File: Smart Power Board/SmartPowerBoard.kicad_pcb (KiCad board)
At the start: 4 copper layers, 41.8 x 41.5 mm, 94 parts, among them J1 430450200, J2 USB_C_Receptacle_USB2.0_16P, J3 430450200, J4 Conn_01x02_Socket, J5 Screw_Terminal_01x02, J6 Screw_Terminal_01x02, Q1 PMOS, Q2 NMOS, SW1 SW_Push, SW2 SW_Push, SW3 SW_Push, U1 INA3221, U2 X096-2864TMBAG01-H30, U4 TPS56C230RJER, U5 TPS56C230RJER, U6 RP2040, U7 W25Q32JVSS, Y1 FL1200138

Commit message: Feat[SmartPowerBoard]: New Layout
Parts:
- removed J4: Conn_01x02_Socket, Connector_Molex:Molex_PicoBlade_53047-0210_1x02_P1.25mm_Vertical
- removed J6: Screw_Terminal_01x02, 282837_2:TE_282837-2
- J3: value 430450200 -> 430450601; footprint ul_430450200:CON_430450200_MOL -> 430450601:MOLEX_430450601
- J5: value Screw_Terminal_01x02 -> 430450400; footprint 282837_2:TE_282837-2 -> 430450400:MOLEX_430450400
- moved J2 37.8 mm to (169.2, 122.0), turned to 0 degrees
- moved J5 33.9 mm to (154.2, 85.0), turned to 180 degrees
- moved Y1 28.1 mm to (160.6, 123.3), turned to 90 degrees
- moved R10 27.5 mm to (167.2, 116.6), turned to 180 degrees
- moved R11 27.5 mm to (171.1, 116.6)
- moved C34 26.1 mm to (159.3, 119.9), turned to 180 degrees
- moved R34 26.0 mm to (158.0, 118.2), turned to 90 degrees
- moved C33 25.1 mm to (161.3, 121.0), turned to 180 degrees
- moved R38 25.0 mm to (156.0, 112.0), turned to 90 degrees
- moved R35 24.8 mm to (159.0, 118.2), turned to 90 degrees
- moved R37 24.5 mm to (156.0, 110.0), turned to -90 degrees
- moved R19 24.0 mm to (161.3, 119.9), turned to 180 degrees
- moved C12 22.9 mm to (160.9, 118.4), turned to 90 degrees
- moved C13 22.6 mm to (157.3, 107.9), turned to -90 degrees
- moved SW3 22.4 mm to (168.8, 85.9), turned to 180 degrees
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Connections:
- J1 pad 1: GND -> unconnected-(J1-Pad1)
- J3 pad 2: /Triple Channel Monitor/12V_{OUT} -> GND
- J5 pad 2: /Triple Channel Monitor/5V_{OUT} -> GND
- R13 pad 4: /Buck Converter 5V/V_{OUT} -> /Triple Channel Monitor/5V_{IN}
- R14 pad 1: /12V_{IN} -> /Triple Channel Monitor/12V_{IN}
- R14 pad 2: Net-(U1-IN-1) -> Net-(U1-IN-3)
- R14 pad 3: Net-(U1-IN+1) -> Net-(U1-IN+3)
- R15 pad 2: Net-(U1-IN-3) -> Net-(U1-IN-1)
- R15 pad 3: Net-(U1-IN+3) -> Net-(U1-IN+1)
- R27 pad 2: Net-(U5-VCC) -> /Buck Converter 3.3V/V_{CC}
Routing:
- net /12V_{IN}: track 53.8 -> 0.00 mm, vias 3 -> 0
- net /3.3V_{IN}: track 23.3 -> 0.00 mm, vias 2 -> 0
- net /MCU/USB_M: track 22.6 -> 0.00 mm
- net /Triple Channel Monitor/3.3V_{IN}: track 21.9 -> 0.00 mm, vias 3 -> 0
- net /Triple Channel Monitor/12V_{OUT}: track 20.8 -> 0.00 mm, vias 1 -> 0
- net /Triple Channel Monitor/5V_{OUT}: track 19.0 -> 0.00 mm, vias 1 -> 0
- net /MCU/USB_P: track 15.9 -> 0.00 mm
- net /Buck Converter 5V/V_{OUT}: track 13.5 -> 0.00 mm, vias 2 -> 0
- net /Triple Channel Monitor/3.3V: track 13.5 -> 0.02 mm, vias 3 -> 1
- net /MCU/3.3V: track 12.9 -> 0.00 mm, vias 1 -> 0
- net Net-(Q1-G): track 11.7 -> 0.00 mm
- net Net-(U5-VCC): track 10.7 -> 0.00 mm, vias 2 -> 0
- net /MCU/XIN: track 8.49 -> 0.00 mm
- net Net-(U6-USB_DM): track 7.72 -> 0.00 mm, vias 2 -> 0
- net Net-(U6-USB_DP): track 7.31 -> 0.00 mm, vias 2 -> 0
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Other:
- board size 41.8 x 41.5 mm -> 38.7 x 49.5 mm
- board text added: "YOU CAN CHANGE THIS"

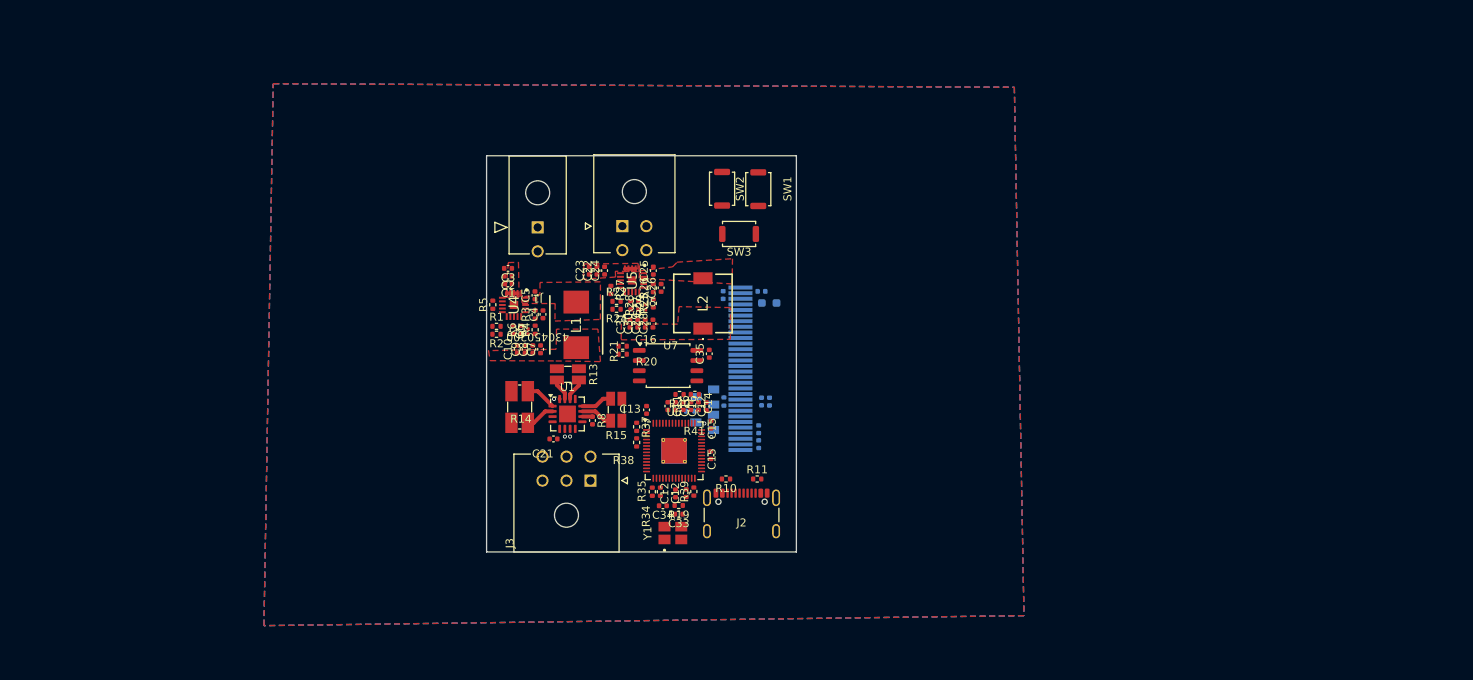
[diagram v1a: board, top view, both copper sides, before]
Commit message: Feat[SmartPowerBoard]: Organized Schematic and New Buck
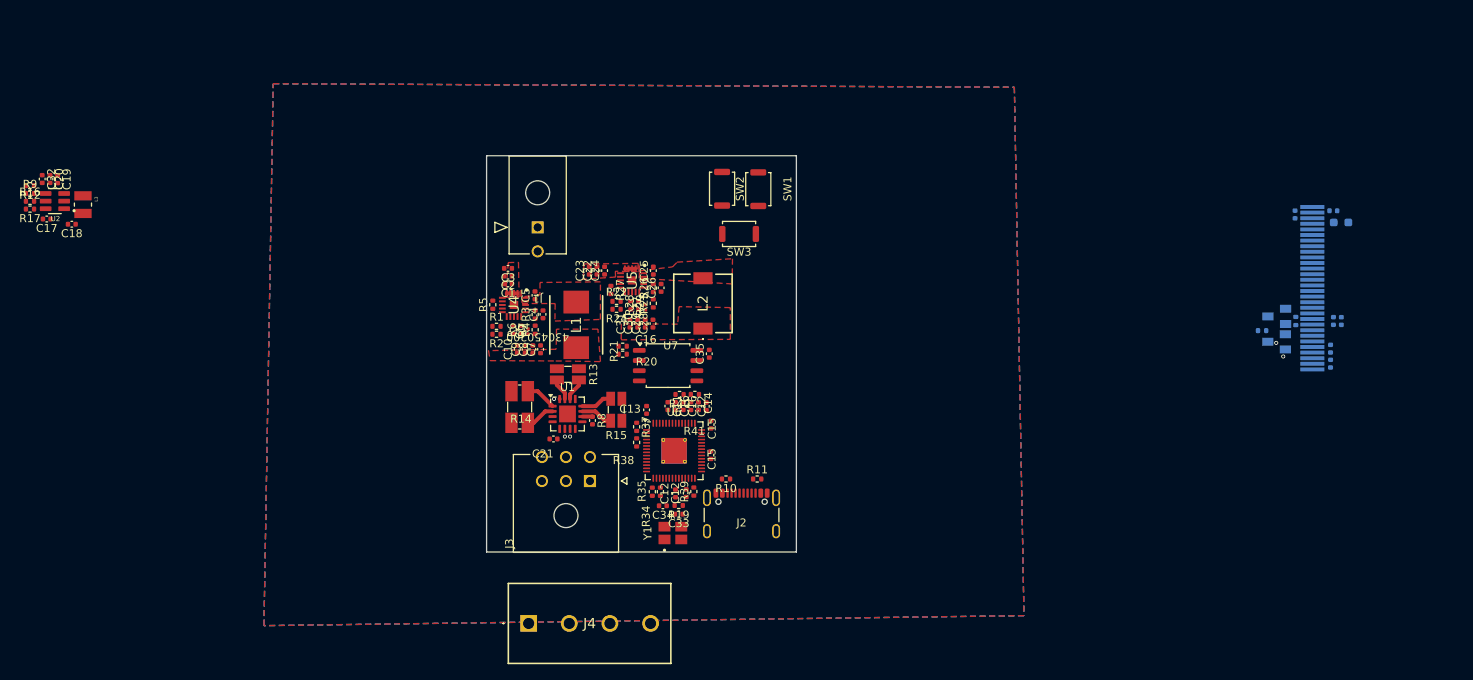
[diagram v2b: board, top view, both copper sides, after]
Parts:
- removed J5: 430450400, 430450400:MOLEX_430450400
- added C17: 0.1uF, Capacitor_SMD:C_0402_1005Metric, F.Cu at (82.3, 84.1)
- added C18: 47uF, Capacitor_SMD:C_0402_1005Metric, F.Cu at (85.4, 84.7)
- added C19: 22uF, Capacitor_SMD:C_0402_1005Metric, F.Cu at (83.7, 79.1)
- added C20: 22uF, Capacitor_SMD:C_0402_1005Metric, F.Cu at (82.7, 79.1)
- added C32: 0.1uF, Capacitor_SMD:C_0402_1005Metric, F.Cu at (81.7, 79.1)
- added J4: Screw_Terminal_01x04, 282857-4_KiCad:2828574, F.Cu at (142.5, 134.6)
- added L3: MLP2520S3R3ST0S1, MLP2520S3R3ST0S1:INDC2520X120N, F.Cu at (86.8, 82.3)
- added R12: 10k, Resistor_SMD:R_0402_1005Metric, F.Cu at (80.2, 79.9)
- added R16: 102k, Resistor_SMD:R_0402_1005Metric, F.Cu at (80.2, 81.9)
- added R17: 51k, Resistor_SMD:R_0402_1005Metric, F.Cu at (80.2, 82.8)
- added R9: 33.2k, Resistor_SMD:R_0402_1005Metric, F.Cu at (80.2, 80.9)
- added U2: TPS561201DDCR, TPS561201DDCR:SOT95P280X110-6N, F.Cu at (83.3, 81.8)
- moved Q2 72.2 mm to (236.1, 96.2)
- moved R18 72.2 mm to (238.4, 96.8)
- moved C17 72.2 mm to (243.1, 83.0)
- moved C18 72.2 mm to (238.3, 83.5)
- moved C19 72.2 mm to (242.8, 102.2)
- moved C20 72.2 mm to (242.8, 100.3)
- moved C32 72.2 mm to (244.1, 96.8)
- moved C36 72.2 mm to (243.1, 96.8)
- moved Q1 72.2 mm to (236.0, 99.4)
- moved R12 72.2 mm to (234.2, 98.0)
- moved R9 72.2 mm to (244.1, 84.5)
- moved U2 72.2 mm to (241.3, 92.8)
- moved J3 0.08 mm to (150.2, 116.8)
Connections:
- net /MCU/5V renamed /MCU/5V_{IN}
- C1 pad 1: /Buck Converter 5V/V_{IN} -> /12V_{IN}
- C10 pad 1: /Buck Converter 5V/V_{OUT} -> /Buck Converter 5V/5V_{OUT}
- C13 pad 2: /MCU/3.3V -> /MCU/3.3V_{CC}
- C14 pad 2: /MCU/3.3V -> /MCU/3.3V_{CC}
- C15 pad 2: /MCU/3.3V -> /MCU/3.3V_{CC}
- C16 pad 2: /MCU/3.3V -> /MCU/3.3V_{CC}
- C2 pad 1: /Buck Converter 5V/V_{IN} -> /12V_{IN}
- C21 pad 2: /Triple Channel Monitor/3.3V -> /MCU/3.3V_{CC}
- C22 pad 1: /Buck Converter 3.3V/V_{IN} -> /12V_{IN}
- C23 pad 1: /Buck Converter 3.3V/V_{IN} -> /12V_{IN}
- C24 pad 1: /Buck Converter 3.3V/V_{IN} -> /12V_{IN}
- C27 pad 1: /Buck Converter 3.3V/V_{OUT} -> /Buck Converter 3.3V/3.3V_{OUT}
- C28 pad 1: /Buck Converter 3.3V/V_{OUT} -> /Buck Converter 3.3V/3.3V_{OUT}
- C29 pad 1: /Buck Converter 3.3V/V_{OUT} -> /Buck Converter 3.3V/3.3V_{OUT}
- C3 pad 1: /Buck Converter 5V/V_{IN} -> /12V_{IN}
- C30 pad 1: /Buck Converter 3.3V/V_{OUT} -> /Buck Converter 3.3V/3.3V_{OUT}
- C31 pad 1: /Buck Converter 3.3V/V_{OUT} -> /Buck Converter 3.3V/3.3V_{OUT}
- C35 pad 2: /MCU/3.3V -> /MCU/3.3V_{CC}
- C6 pad 1: /Buck Converter 5V/V_{OUT} -> /Buck Converter 5V/5V_{OUT}
- C7 pad 1: /Buck Converter 5V/V_{OUT} -> /Buck Converter 5V/5V_{OUT}
- C8 pad 1: /Buck Converter 5V/V_{OUT} -> /Buck Converter 5V/5V_{OUT}
- C9 pad 1: /Buck Converter 5V/V_{OUT} -> /Buck Converter 5V/5V_{OUT}
- J1 pad 1: unconnected-(J1-Pad1) -> GND
- J3 pad 4: /3.3V_{IN} -> /12V_{OUT}
- J3 pad 5: /5V_{OUT} -> /12V_{OUT}
- J3 pad 6: /12V_{IN} -> /12V_{OUT}
- L1 pad 2: /Buck Converter 5V/V_{OUT} -> /Buck Converter 5V/5V_{OUT}
- L2 pad 1: /Buck Converter 3.3V/V_{OUT} -> /Buck Converter 3.3V/3.3V_{OUT}
- R1 pad 1: /Buck Converter 5V/V_{IN} -> /12V_{IN}
- R13 pad 4: /Triple Channel Monitor/5V_{IN} -> /Buck Converter 5V/5V_{OUT}
- R14 pad 1: /Triple Channel Monitor/12V_{IN} -> /12V_{IN}
- R15 pad 4: /Triple Channel Monitor/3.3V_{IN} -> /Buck Converter 3.3V/3.3V_{OUT}
- R21 pad 2: /MCU/3.3V -> /MCU/3.3V_{CC}
- R22 pad 1: /Buck Converter 3.3V/V_{IN} -> /12V_{IN}
- R28 pad 1: /Buck Converter 3.3V/V_{OUT} -> /Buck Converter 3.3V/3.3V_{OUT}
- R34 pad 1: /MCU/3.3V -> /MCU/3.3V_{CC}
- R35 pad 1: /MCU/3.3V -> /MCU/3.3V_{CC}
- R37 pad 1: /MCU/3.3V -> /MCU/3.3V_{CC}
- R37 pad 2: /MCU/SDA -> /MCU/SCL
- R38 pad 1: /MCU/3.3V -> /MCU/3.3V_{CC}
- R38 pad 2: /MCU/SCL -> /MCU/SDA
- R39 pad 1: /MCU/3.3V -> /MCU/3.3V_{CC}
- R6 pad 1: /Buck Converter 5V/V_{OUT} -> /Buck Converter 5V/5V_{OUT}
- R8 pad 2: /Triple Channel Monitor/3.3V -> /MCU/3.3V_{CC}
- U1 pad 16: /Triple Channel Monitor/3.3V -> /MCU/3.3V_{CC}
- U1 pad 4: /Triple Channel Monitor/3.3V -> /MCU/3.3V_{CC}
- U1 pad 6: /Triple Channel Monitor/SCL -> /MCU/SCL
- U1 pad 7: /Triple Channel Monitor/SDA -> /MCU/SDA
- U1 pad 8: /Triple Channel Monitor/WARN -> /MCU/WARN
- U1 pad 9: /Triple Channel Monitor/CRIT -> /MCU/CRIT
- U4 pad 2: /Buck Converter 5V/V_{IN} -> /12V_{IN}
- U4 pad 3: /Buck Converter 5V/V_{IN} -> /12V_{IN}
- U4 pad 4: /Buck Converter 5V/V_{IN} -> /12V_{IN}
- U4 pad 5: /Buck Converter 5V/V_{IN} -> /12V_{IN}
- U5 pad 2: /Buck Converter 3.3V/V_{IN} -> /12V_{IN}
- U5 pad 3: /Buck Converter 3.3V/V_{IN} -> /12V_{IN}
- U5 pad 4: /Buck Converter 3.3V/V_{IN} -> /12V_{IN}
- U5 pad 5: /Buck Converter 3.3V/V_{IN} -> /12V_{IN}
- U6 pad 1: /MCU/3.3V -> /MCU/3.3V_{CC}
- U6 pad 10: /MCU/3.3V -> /MCU/3.3V_{CC}
- U6 pad 2: /MCU/SDA -> /MCU/SCL
- U6 pad 22: /MCU/3.3V -> /MCU/3.3V_{CC}
- U6 pad 3: /MCU/SCL -> /MCU/SDA
- U6 pad 33: /MCU/3.3V -> /MCU/3.3V_{CC}
- U6 pad 42: /MCU/3.3V -> /MCU/3.3V_{CC}
- U6 pad 43: /MCU/3.3V -> /MCU/3.3V_{CC}
- U6 pad 44: /MCU/3.3V -> /MCU/3.3V_{CC}
- U6 pad 48: /MCU/3.3V -> /MCU/3.3V_{CC}
- U6 pad 49: /MCU/3.3V -> /MCU/3.3V_{CC}
- U7 pad 8: /MCU/3.3V -> /MCU/3.3V_{CC}
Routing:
- net /12V_{IN}: track 0.00 -> 2.63 mm
- net /Buck Converter 5V/V_{IN}: track 1.31 -> 0.00 mm
- net /Buck Converter 3.3V/V_{IN}: track 1.31 -> 0.00 mm
- net /Triple Channel Monitor/3.3V: track 0.02 -> 0.00 mm, vias 1 -> 0
- net /MCU/3.3V_{CC}: track 0.00 -> 0.02 mm, vias 0 -> 1
- net /Triple Channel Monitor/SDA: vias 1 -> 0
- net /Triple Channel Monitor/SCL: vias 1 -> 0
- net /MCU/SDA: vias 0 -> 1
- net /MCU/SCL: vias 0 -> 1
- added copper zone on F.Cu, net /12V_{IN}
- added copper zone on F.Cu, net /Buck Converter 3.3V/3.3V_{OUT}
- added copper zone on F.Cu, net /Buck Converter 5V/5V_{OUT}
- removed copper zone on F.Cu, net /Buck Converter 3.3V/V_{IN}
- removed copper zone on F.Cu, net /Buck Converter 3.3V/V_{OUT}
- removed copper zone on F.Cu, net /Buck Converter 5V/V_{IN}
- removed copper zone on F.Cu, net /Buck Converter 5V/V_{OUT}
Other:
- board text added: "Add mini buck"
- board text added: "NEW OLED"
- board text removed: "YOU CAN CHANGE THIS"

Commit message: Feat[SmartPowerBoard]: Internal Power + OLED
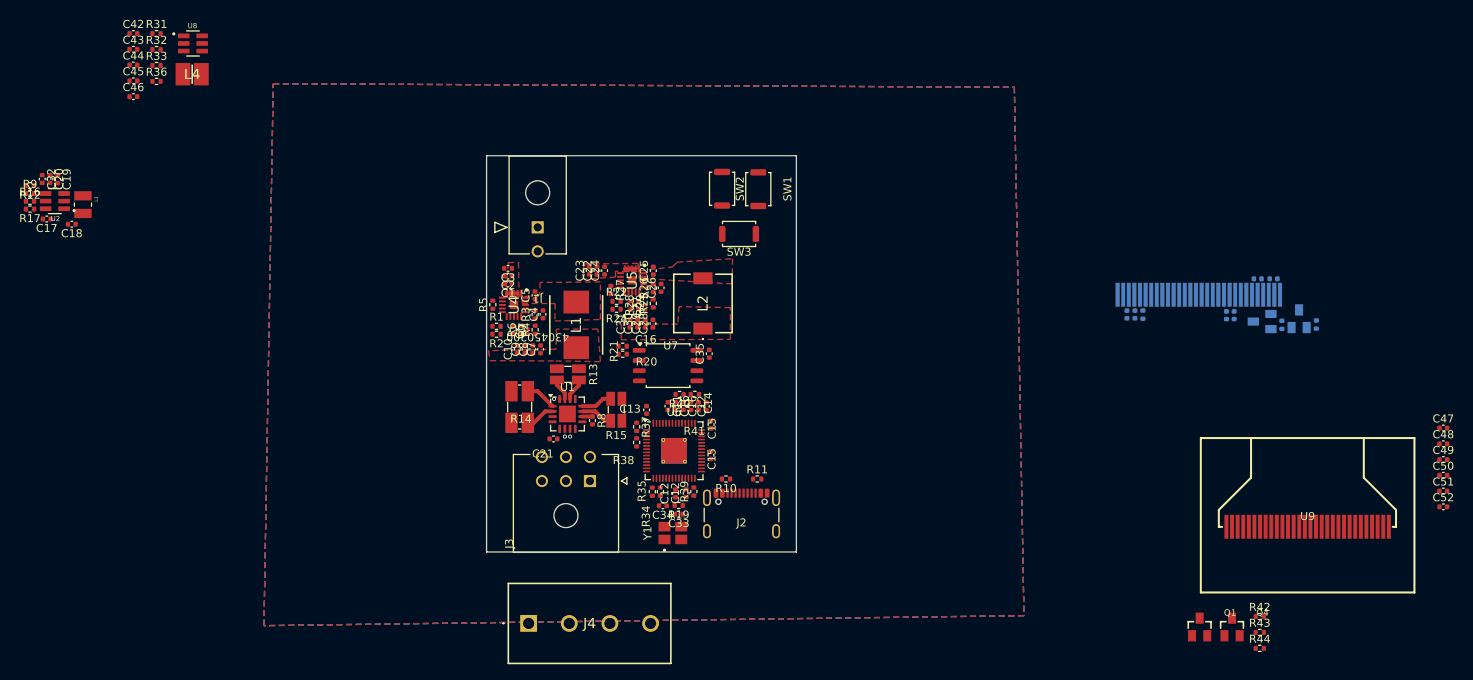
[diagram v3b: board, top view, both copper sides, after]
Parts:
- removed the C17 at (243.1, 83.0)
- removed the C18 at (238.3, 83.5)
- removed the C19 at (242.8, 102.2)
- removed the C20 at (242.8, 100.3)
- removed the C32 at (244.1, 96.8)
- removed the R12 at (234.2, 98.0)
- removed the R9 at (244.1, 84.5)
- removed the U2 at (241.3, 92.8)
- added C37: 4.7uF, Capacitor_SMD:C_0402_1005Metric, B.Cu at (218.3, 96.0)
- added C38: 1uF, Capacitor_SMD:C_0402_1005Metric, B.Cu at (229.8, 96.1)
- added C39: 1uF, Capacitor_SMD:C_0402_1005Metric, B.Cu at (230.7, 96.1)
- added C40: 1uF, Capacitor_SMD:C_0402_1005Metric, B.Cu at (235.6, 91.5)
- added C41: 1uF, Capacitor_SMD:C_0402_1005Metric, B.Cu at (233.7, 91.5)
- added C42: 22uF, Capacitor_SMD:C_0402_1005Metric, F.Cu at (93.1, 60.9)
- added C43: 22uF, Capacitor_SMD:C_0402_1005Metric, F.Cu at (93.1, 62.9)
- added C44: 0.1uF, Capacitor_SMD:C_0402_1005Metric, F.Cu at (93.1, 64.8)
- added C45: 0.1uF, Capacitor_SMD:C_0402_1005Metric, F.Cu at (93.1, 66.8)
- added C46: 47uF, Capacitor_SMD:C_0402_1005Metric, F.Cu at (93.1, 68.8)
- added C47: 1uF, Capacitor_SMD:C_0402_1005Metric, F.Cu at (256.9, 110.2)
- added C48: 1uF, Capacitor_SMD:C_0402_1005Metric, F.Cu at (256.9, 112.2)
- added C49: 4.7uF, Capacitor_SMD:C_0402_1005Metric, F.Cu at (256.9, 114.1)
- added C50: 2.2uF, Capacitor_SMD:C_0402_1005Metric, F.Cu at (256.9, 116.1)
- added C51: 1uF, Capacitor_SMD:C_0402_1005Metric, F.Cu at (256.9, 118.1)
- added C52: 1uF, Capacitor_SMD:C_0402_1005Metric, F.Cu at (256.9, 120.0)
- added L4: SRP3212A-4R7M, SRP3212A-4R7M_KiCad:INDC3225X120N, F.Cu at (100.5, 66.0)
- added Q3: FDN335N, FDN335N:SSOT-3, B.Cu at (238.8, 96.5)
- added Q4: FDN335N, FDN335N:SSOT-3, F.Cu at (230.5, 135.1)
- added R23: 47k, Resistor_SMD:R_0402_1005Metric, B.Cu at (236.7, 97.3)
- added R30: 47k, Resistor_SMD:R_0402_1005Metric, B.Cu at (241.0, 97.3)
- added R31: 102k, Resistor_SMD:R_0402_1005Metric, F.Cu at (96.0, 60.9)
- added R32: 51k, Resistor_SMD:R_0402_1005Metric, F.Cu at (96.0, 62.9)
- added R33: 42.2k, Resistor_SMD:R_0402_1005Metric, F.Cu at (96.0, 64.9)
- added R36: 10k, Resistor_SMD:R_0402_1005Metric, F.Cu at (96.0, 66.9)
- added R42: 47k, Resistor_SMD:R_0402_1005Metric, F.Cu at (233.9, 133.8)
- added R43: 620k, Resistor_SMD:R_0402_1005Metric, F.Cu at (233.9, 135.8)
- added R44: 47k, Resistor_SMD:R_0402_1005Metric, F.Cu at (233.9, 137.7)
- added U3: ~, LIB_X096-2864TMBAG01-H30:X096-2864TMBAG01-H30, B.Cu at (226.3, 92.7)
- added U8: TPS561201DDCR, TPS561201DDCR:SOT95P280X110-6N, F.Cu at (100.6, 62.1)
- added U9: ~, LIB_X096-2864TMBAG01-H30:X096-2864TMBAG01-H30, F.Cu at (239.9, 121.7)
- C36: value 1uF -> 2.2uF
- Q1: value PMOS -> FDN338P; moved to F.Cu
- Q2: value NMOS -> FDN338P; footprint FDN335N:SSOT-3 -> FDN338P:SSOT-3
- R18: value 47k -> 620k
- moved Q1 36.9 mm to (226.4, 135.1), turned to 0 degrees
- moved C36 25.8 mm to (217.3, 96.0), turned to 90 degrees
- moved R18 19.1 mm to (219.3, 96.0)
- moved Q2 1.94 mm to (234.2, 96.9)
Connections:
- C36 pad 1: /MCU/VDD -> GND
- C36 pad 2: GND -> Net-(U3-VCC)
- Q1 pad 1: /MCU/VBAT -> Net-(Q1-Pad1)
- Q1 pad 2: Net-(Q1-G) -> /Inner Buck Converter 4V/4V_{CC}
- Q1 pad 3: /MCU/V_{IN} -> /OLED Display/V_{BAT}
- Q2 pad 1: Net-(Q1-G) -> Net-(Q2-Pad1)
- Q2 pad 2: /MCU/GPIO -> /MCU/V_{IN}
- Q2 pad 3: GND -> /MCU/V_{BAT}
- R18 pad 1: /MCU/GPIO -> GND
- R18 pad 2: GND -> Net-(U3-IREF)
- U6 pad 6: unconnected-(U6-GPIO4-Pad6) -> /MCU/GPIO4
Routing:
- net (no net): vias 2 -> 0
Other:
- board text removed: "Add mini buck"
- board text removed: "NEW OLED"
